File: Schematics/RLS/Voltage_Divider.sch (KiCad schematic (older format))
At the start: 6 parts

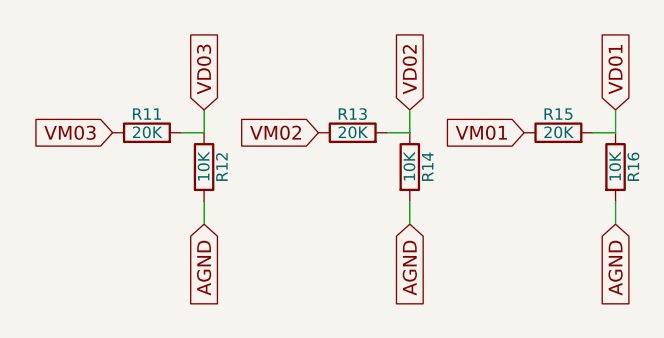
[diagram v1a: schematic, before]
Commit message: Updated Schematic (Almost Done)
Finished both variable regulator circuits, added connectors for LAs, added +/- 5 regulated circuit for DB +/- 5V (needs to be tested before PCB implementation), various renaming and labeling
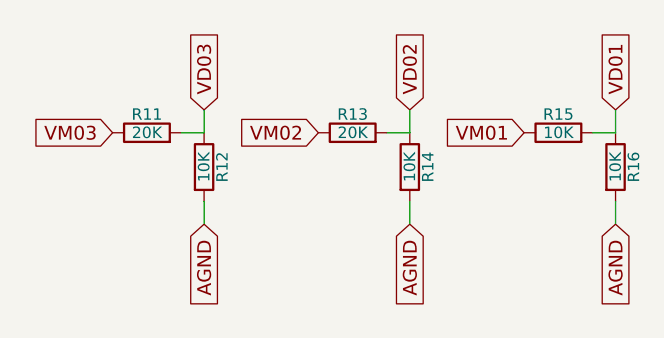
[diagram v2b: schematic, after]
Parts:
- R15: value 20K -> 10K
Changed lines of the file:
@@
 $Descr A4 11693 8268
 encoding utf-8
-Sheet 2 5
+Sheet 2 7
 Title ""
 Date ""
@@
 P 5950 2100
 F 0 "R15" V 6030 2100 50  0000 C CNN
-F 1 "20K" V 5950 2100 50  0000 C CNN
+F 1 "10K" V 5950 2100 50  0000 C CNN
 F 2 "" V 5880 2100 50  0001 C CNN
 F 3 "" H 5950 2100 50  0001 C CNN
